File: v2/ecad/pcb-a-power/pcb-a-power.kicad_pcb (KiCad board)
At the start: 4 copper layers, 285 x 160 mm, 113 parts, among them U10 TPS2065CDBV, U11 INA219AIDCN, U12 USBLC6-2SC6, U13 TPS2065CDBV, U14 INA219AIDCN, U15 USBLC6-2SC6, U16 TPS2065CDBV, U17 INA219AIDCN, U18 USBLC6-2SC6, U19 PCA9555PW (0x21), U5 AMS1117-3.3, U6 FE1.1s, U7 TPS2065CDBV, U8 INA219AIDCN, U9 USBLC6-2SC6, Y1 12 MHz 3225

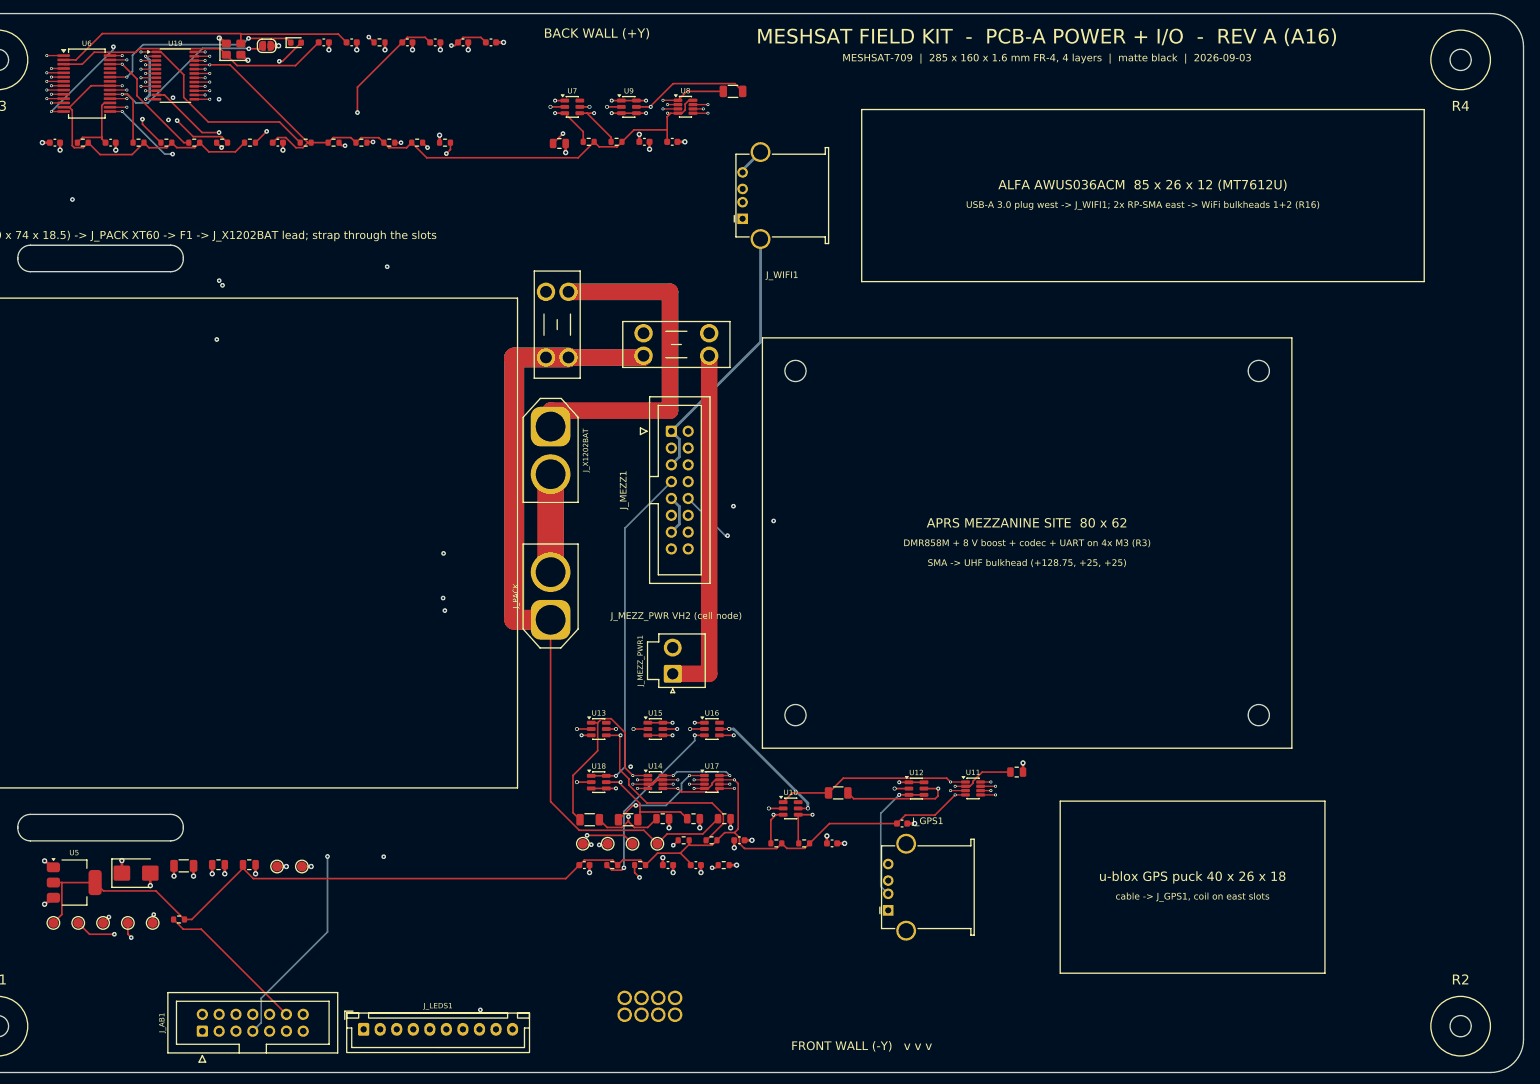
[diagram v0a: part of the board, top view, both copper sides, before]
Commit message: chore(ecad): A17 and B11 project files as routed and finished [MESHSAT-709]
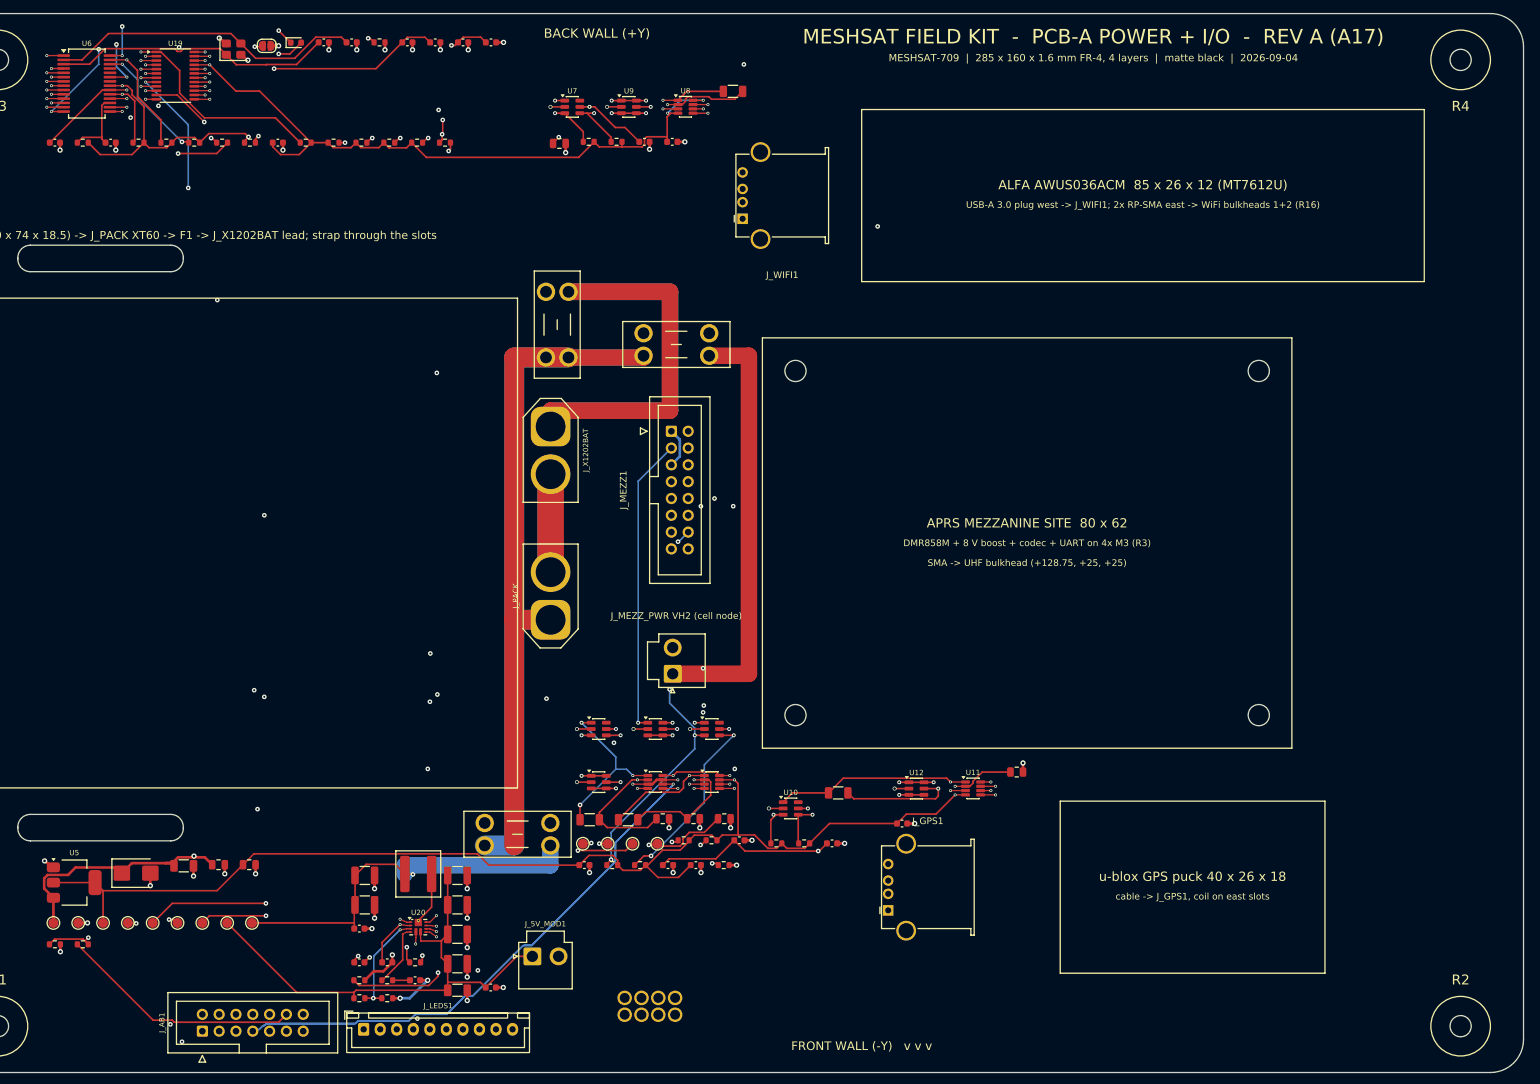
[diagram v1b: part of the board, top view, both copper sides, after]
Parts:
- removed R12: 10k, R_0603_1608Metric
- added C38: 100n 25V, C_0603_1608Metric, F.Cu at (94.1, 173.4)
- added C39: 1u, C_0603_1608Metric, F.Cu at (98.3, 173.4)
- added C40: 4.7n, C_0603_1608Metric, F.Cu at (102.5, 176.1)
- added C41: 22u 10V X7R 1210, C_1210_3225Metric, F.Cu at (94.9, 160.2)
- added C42: 22u 10V X7R 1210, C_1210_3225Metric, F.Cu at (94.9, 164.7)
- added C43: 100n, C_0603_1608Metric, F.Cu at (94.1, 168.3)
- added C44: 22u 10V X7R 1210, C_1210_3225Metric, F.Cu at (108.9, 160.2)
- added C45: 22u 10V X7R 1210, C_1210_3225Metric, F.Cu at (108.9, 164.7)
- added C46: 22u 10V X7R 1210, C_1210_3225Metric, F.Cu at (108.9, 169.1)
- added C47: 22u 10V X7R 1210, C_1210_3225Metric, F.Cu at (108.9, 173.6)
- added C48: 100n, C_0603_1608Metric, F.Cu at (114.0, 177.2)
- added C49: 100u 10V, C_1206_3216Metric, F.Cu at (108.9, 177.6)
- added F3: 15 A mini blade (Keystone 3568 holder): pack node to the 5 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, Fuseholder_Blade_Mini_Keystone_3568, F.Cu at (113.0, 152.3)
- added J_5V_MOD1: 5 V module rail to PCB-B J_5V_MOD (JST-VH, 18 AWG): + -, JST_VH_B2P-VH_1x02_P3.96mm_Vertical, F.Cu at (120.2, 172.4)
- added L2: 1.5uH XAL6030-152MEB (Isat 12 A, 5.6 mOhm), L_Coilcraft_XAL6030-XXX, F.Cu at (103.0, 160.0)
- added R44: 301k 1% (500 kHz), R_0603_1608Metric, F.Cu at (102.5, 173.4)
- added R45: 100k 1% (ILIM 10 A peak, 9 A min), R_0603_1608Metric, F.Cu at (94.1, 176.1)
- added R46: 17.4k, R_0603_1608Metric, F.Cu at (98.3, 176.1)
- added R47: 63.4k 1%, R_0603_1608Metric, F.Cu at (94.1, 178.8)
- added R48: 20k 1%, R_0603_1608Metric, F.Cu at (98.3, 178.8)
- added R49: 100k, R_0603_1608Metric, F.Cu at (48.1, 170.6)
- added R50: 10k, R_0603_1608Metric, F.Cu at (52.3, 170.6)
- added TP12: +5V_MOD, TestPoint_Pad_D1.5mm, F.Cu at (74.1, 167.4)
- added TP13: BOOST_CELL, TestPoint_Pad_D1.5mm, F.Cu at (77.9, 167.4)
- added U20: TPS61089 boost 5.05 V module rail, Texas_VQFN-RNR0011A-11, F.Cu at (103.0, 168.0)
- moved TP1 34.9 mm to (47.9, 167.4)
- moved TP2 34.9 mm to (51.6, 167.4)
- moved TP10 7.50 mm to (66.6, 167.4)
- moved TP11 7.50 mm to (70.4, 167.4)
- moved TP3 7.50 mm to (55.4, 167.4)
- moved TP6 7.50 mm to (59.1, 167.4)
- moved TP7 7.50 mm to (62.9, 167.4)
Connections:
- C22 pad 1: +5V -> /+5V_MOD
- C34 pad 1: +5V -> /+5V_MOD
- C35 pad 1: +5V -> /+5V_MOD
- C36 pad 1: +5V -> /+5V_MOD
- C37 pad 1: +5V -> /+5V_MOD
- J_AB1 pad 12: /BANK_ALERT -> /X1202_5V
- R18 pad 1: +5V -> /+5V_MOD
- U10 pad 5: +5V -> /+5V_MOD
- U13 pad 5: +5V -> /+5V_MOD
- U16 pad 5: +5V -> /+5V_MOD
- U6 pad 20: +5V -> /+5V_MOD
- U7 pad 5: +5V -> /+5V_MOD
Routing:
- net /+5V_MOD: track 0.00 -> 400.0 mm, vias 0 -> 9
- net +5V: track 422.4 -> 63.9 mm, vias 16 -> 1
- net /BOOST_CELL: track 0.00 -> 95.5 mm, vias 0 -> 2
- net /CELL+: track 247.2 -> 340.1 mm, vias 0 -> 1
- net GND: track 697.6 -> 789.1 mm, vias 50 -> 64
- net /MOD_EN: track 0.00 -> 64.7 mm, vias 0 -> 2
- net /EN_GPS: track 182.2 -> 220.3 mm, vias 3 -> 4
- net /X1202_5V: track 0.00 -> 37.0 mm
- net /USB_GPS_P: track 215.6 -> 249.3 mm, vias 3 -> 4
- net /EN_UART: track 185.3 -> 213.9 mm
- net /SW5: track 0.00 -> 26.0 mm, vias 0 -> 2
- net +3V3: track 419.2 -> 443.4 mm, vias 9 -> 11
- net /BANK_ALERT: track 23.0 -> 0.00 mm
- net /ILIM5: track 0.00 -> 22.4 mm, vias 0 -> 2
- net /EN_CODEC: track 164.4 -> 185.4 mm, vias 3 -> 5
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- added copper zone on In2.Cu, net +5V_MOD
- removed copper zone on In2.Cu, net +5V
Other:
- board text added: "MESHSAT FIELD KIT - PCB-A POWER + I/O - REV A (A17)"
- board text added: "MESHSAT-709 | 285 x 160 x 1.6 mm FR-4, 4 layers | matte black | 2026-09-04"
- board text added: "PWR ZONE: 3.3 V LDO, test points; A17: F3 + TPS61089 5 V module-rail boost from the cell node, J_5V_MOD1 (VH) to PCB-B"
- board text removed: "MESHSAT FIELD KIT - PCB-A POWER + I/O - REV A (A16)"
- board text removed: "MESHSAT-709 | 285 x 160 x 1.6 mm FR-4, 4 layers | matte black | 2026-09-03"
- board text removed: "PWR ZONE: 3.3 V LDO, test points (A15: the charger, protection, gauge and boost are gone, the X1202 does it all)"

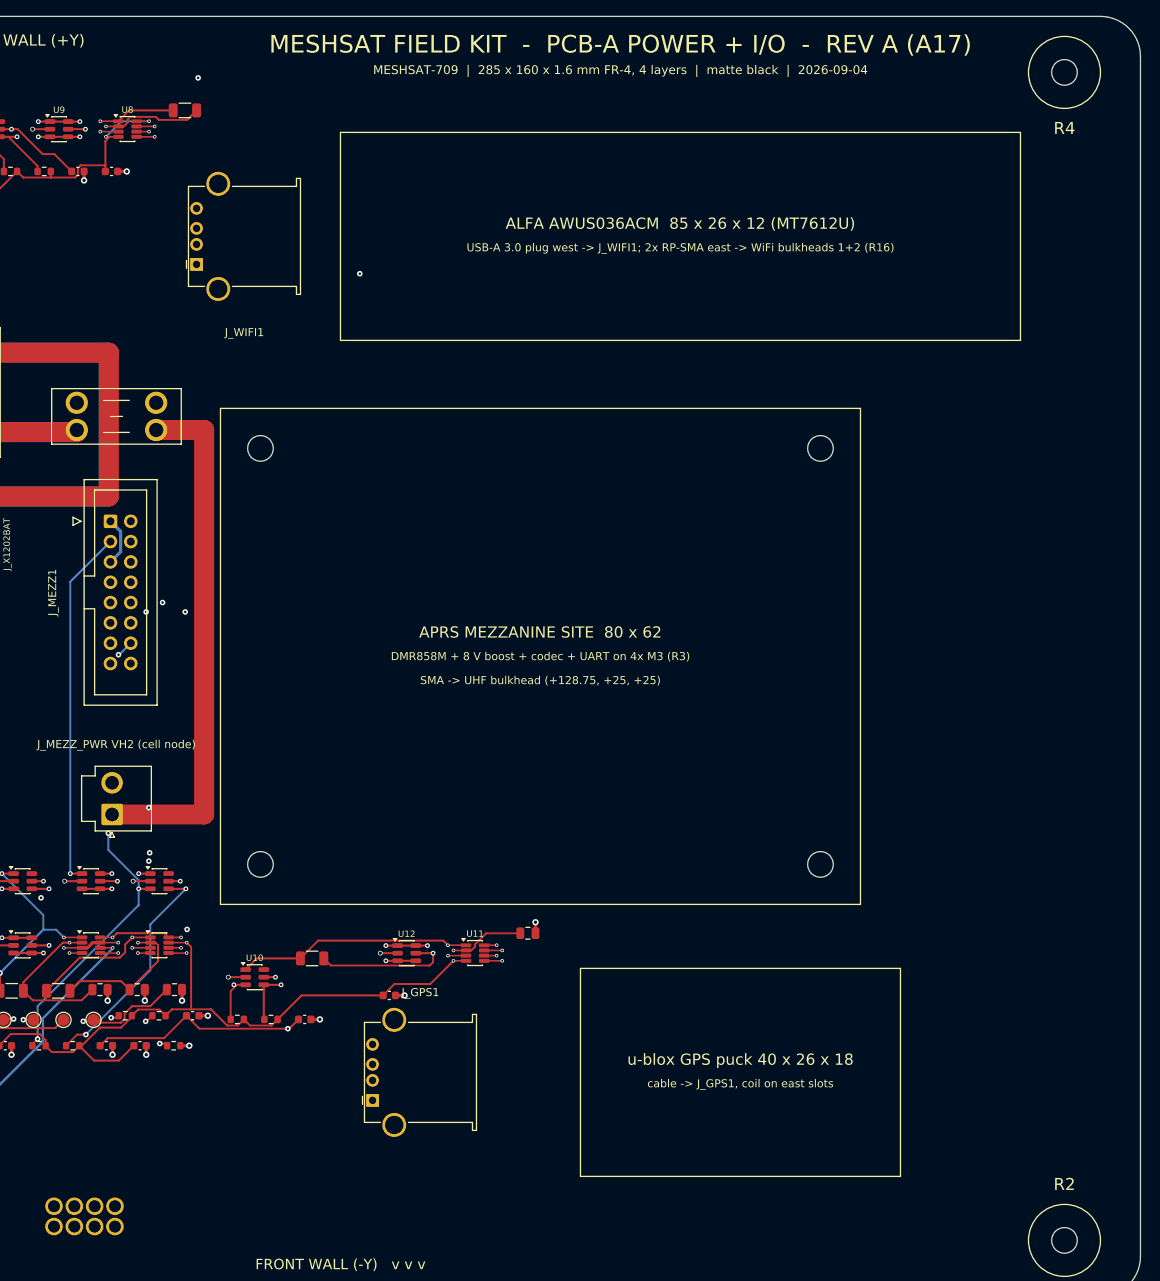
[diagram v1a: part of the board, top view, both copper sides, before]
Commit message: feat(release): A18 (dock holes 1.1 mm for the Preci-Dip 813 connector) and E3 (junction D-hole flat per the Amphenol 132170 drawing), C4 schematic with the switch part numbers, handoff rebuilt, A17 and E2 retired [MESHSAT-709]
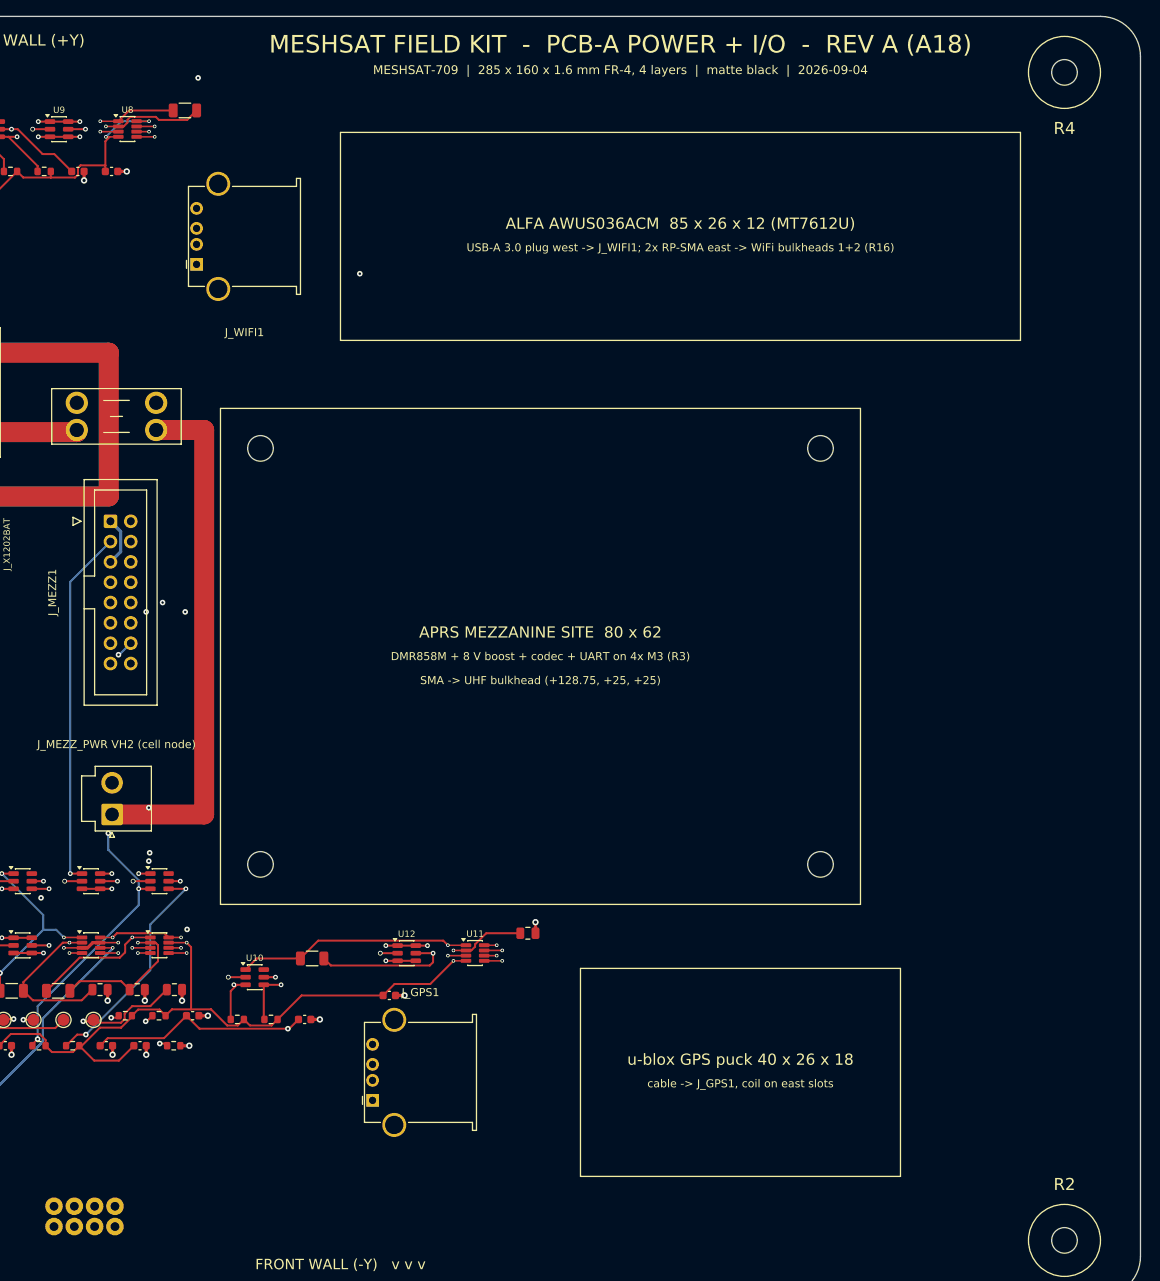
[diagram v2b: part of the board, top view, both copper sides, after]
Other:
- board text added: "MESHSAT FIELD KIT - PCB-A POWER + I/O - REV A (A18)"
- board text removed: "MESHSAT FIELD KIT - PCB-A POWER + I/O - REV A (A17)"
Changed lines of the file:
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@@
 			(at -3.81 1.27)
 			(size 2.2 2.2)
-			(drill 1.5)
+			(drill 1.1)
 			(layers "*.Cu" "*.Mask")
 			(remove_unused_layers no)
@@
 			(at -1.27 1.27)
 			(size 2.2 2.2)
-			(drill 1.5)
+			(drill 1.1)
 			(layers "*.Cu" "*.Mask")
 			(remove_unused_layers no)
@@
 			(at 1.27 1.27)
 			(size 2.2 2.2)
-			(drill 1.5)
+			(drill 1.1)
 			(layers "*.Cu" "*.Mask")
 			(remove_unused_layers no)
@@
 			(at 3.81 1.27)
 			(size 2.2 2.2)
-			(drill 1.5)
+			(drill 1.1)
 			(layers "*.Cu" "*.Mask")
 			(remove_unused_layers no)
@@
 			(at -3.81 -1.27)
 			(size 2.2 2.2)
-			(drill 1.5)
+			(drill 1.1)
 			(layers "*.Cu" "*.Mask")
 			(remove_unused_layers no)
@@
 			(at -1.27 -1.27)
 			(size 2.2 2.2)
-			(drill 1.5)
+			(drill 1.1)
 			(layers "*.Cu" "*.Mask")
 			(remove_unused_layers no)
@@
 			(at 1.27 -1.27)
 			(size 2.2 2.2)
-			(drill 1.5)
+			(drill 1.1)
 			(layers "*.Cu" "*.Mask")
 			(remove_unused_layers no)
@@
 			(at 3.81 -1.27)
 			(size 2.2 2.2)
-			(drill 1.5)
+			(drill 1.1)
 			(layers "*.Cu" "*.Mask")
 			(remove_unused_layers no)
@@
 		)
 	)
-	(gr_text "MESHSAT FIELD KIT  -  PCB-A POWER + I/O  -  REV A (A17)"
+	(gr_text "MESHSAT FIELD KIT  -  PCB-A POWER + I/O  -  REV A (A18)"
 		(at 205 33.5 0)
 		(layer "F.SilkS")
